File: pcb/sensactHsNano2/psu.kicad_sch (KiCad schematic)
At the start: 14 parts, among them U7 MP4420

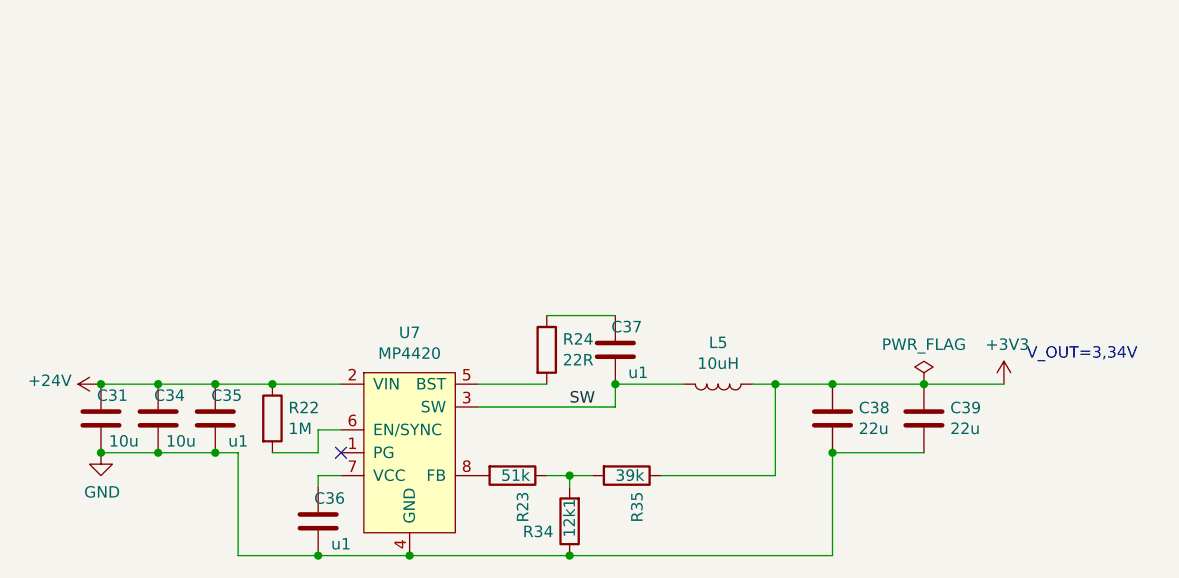
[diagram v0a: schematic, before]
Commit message: DIn-schiene-seitenwand + sensactHsNano2
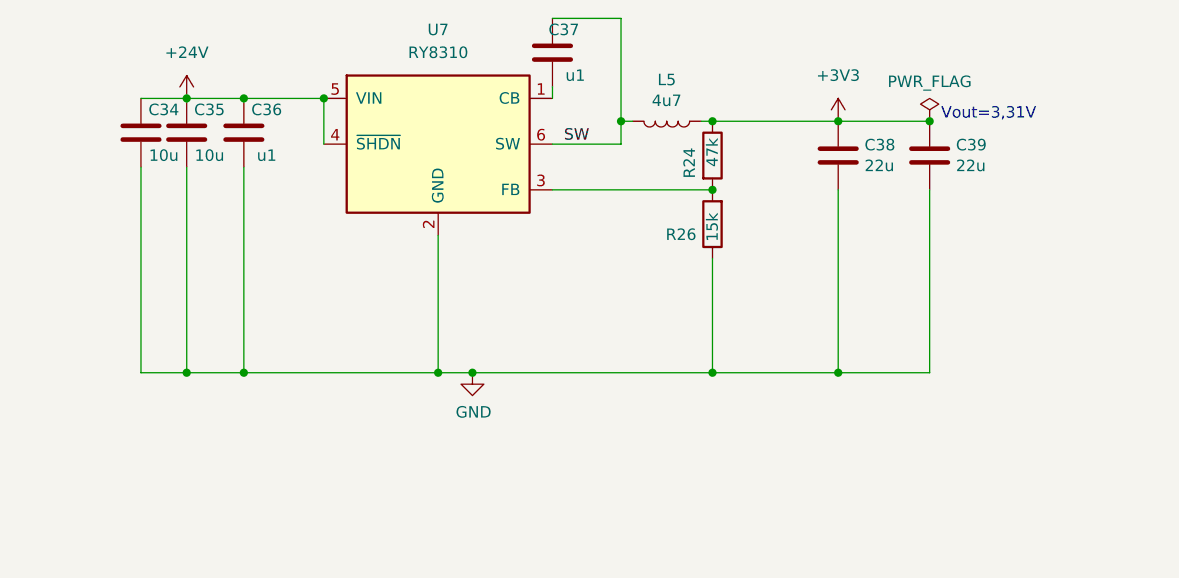
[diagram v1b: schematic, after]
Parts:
- removed C31: 10u, Capacitor_SMD:C_1206_3216Metric, symbol Device:C
- removed R22: 1M, Resistor_SMD:R_0603_1608Metric, symbol Device:R
- removed R23: 51k, Resistor_SMD:R_0603_1608Metric, symbol Device:R
- removed R34: 12k1, Resistor_SMD:R_0603_1608Metric, symbol Device:R
- removed R35: 39k, Resistor_SMD:R_0603_1608Metric, symbol Device:R
- removed U7: MP4420, Package_TO_SOT_SMD:TSOT-23-8, symbol liebler_SEMICONDUCTORS:MP4420
- added R26: 15k, Resistor_SMD:R_0402_1005Metric, symbol Device:R
- added U7: RY8310, Package_TO_SOT_SMD:SOT-23-6, symbol Regulator_Switching:LMR14206
- C34: footprint Capacitor_SMD:C_1206_3216Metric_Pad1.33x1.80mm_HandSolder -> Capacitor_SMD:C_1206_3216Metric
- C35: value u1 -> 10u; footprint Capacitor_SMD:C_0805_2012Metric -> Capacitor_SMD:C_1206_3216Metric
- L5: value 10uH -> 4u7; footprint liebler_PASSIVES:ASPIAIG-Q8080 -> Inductor_SMD:L_Abracon_ASPI-0630LR
- R24: value 22R -> 47k; footprint Resistor_SMD:R_0603_1608Metric -> Resistor_SMD:R_0402_1005Metric
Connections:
- net +24V: now also C36.2, U7.4 (~{SHDN}), U7.5 (VIN)
- net +3V3: now also R24.1
- net GND: now also R26.1, U7.2 (GND)
- net SW: now also C37.2, U7.6 (SW); no longer C37.1
- net at R24.2: now also R26.2, U7.3 (FB)
- new net: C37.1, U7.1 (CB)
- no-connect marks 1 -> 0
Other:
- note added: "Vout=3,31V"
- note removed: "V_OUT=3,34V"
